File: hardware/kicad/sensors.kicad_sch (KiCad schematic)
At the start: 0 parts

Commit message: kicad: chunk #5a - SEN66 reference footprint + 4 zip-tie NPTH + J3 socket
Adds the SEN66 (Sensirion SEN66-SIN-T, MPN 3.001.030, EAN N/A) connection
to the sensors sub-sheet and lays out the mechanical reference + retention
on the PCB. Resolves 2 of 6 expected ERC pin_not_connected (I2C_SDA, SCL).

Schematic (sensors.kicad_sch):
  J3 = JST GH 6-pin board socket (SM06B-GHS-TB compatible). Wiring per
  SEN6x datasheet Table 16: 1=VDD->+3V3, 2=GND, 3=SDA, 4=SCL,
  5=GND-redundant, 6=VDD-redundant (pins 5/6 internally tied to 1/2 in
  the SEN6x). Local 100 nF decoupling (C10) on the cable side of J3.

Custom PCB footprints:
  oas:SEN66_Mechanical_Reference - 55.2 x 25.6 mm body outline on F.Fab +
    F.SilkS, inlet/outlet markers at exact STEP-derived positions
    (inlet 1 obround at SEN66-local 10.7/7.4, inlet 2 rect at 10.65/18.85,
    outlet circle dia 20.74 at 42.4/12.8), connector marker on +X short
    edge, dashed sealing-divider hint at SEN66-local X=26. Mechanical-
    only, no pads (sensor is held by zip-ties, not soldered).
  oas:ZipTieHole_3mm_NPTH - reusable NPTH hole (3 mm drill, 4 mm silk
    ring, no copper) for ZT1..ZT4 mounting holes.

PCB placement (v0.7 of this chunk after user-iterated refinements):
  - SEN66 anchor at PCB (12, 25), rotation 90 CW. Body X 12..37.6,
    Y -30.2..25 -- clears all cutout zones (lowest cutout Y=27.2 at C2)
    by 2.2 mm. Long axis radial, connector edge at PCB top of body.
    Cross-sector placement (per user OK).
  - Zip-tie holes ZT1..ZT4 at SEN66-local (22, +-3) and (30, +-3).
    Both X positions in safe corridor [19.22, 31.03] so a 2 mm
    zip-tie band centred at each X passes over the SEN66 body
    without covering any inlet or outlet on the air-side face.
    PCB-global: ZT1=(9,3), ZT2=(40.6,3), ZT3=(9,-5), ZT4=(40.6,-5).
    All clear of cable pass-through hole (Phi 12) at origin.
  - J3 at PCB (48, 7), rotation 90 (vertical pin row, plug socket
    opening faces SEN66). 10.4 mm to body right edge for cable be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
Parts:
- added C10: 100nF, symbol Device:C
- added J3: JST SM06B-GHS-TB (SEN66-SIN-T, MPN 3.001.030; TME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, symbol Connector_Generic:Conn_01x06
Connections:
- new net +3V3: C10.1, J3.1 (Pin_1), J3.6 (Pin_6)
- new net GND: C10.2, J3.2 (Pin_2), J3.5 (Pin_5)
- new net I2C_SCL: J3.4 (Pin_4)
- new net I2C_SDA: J3.3 (Pin_3)

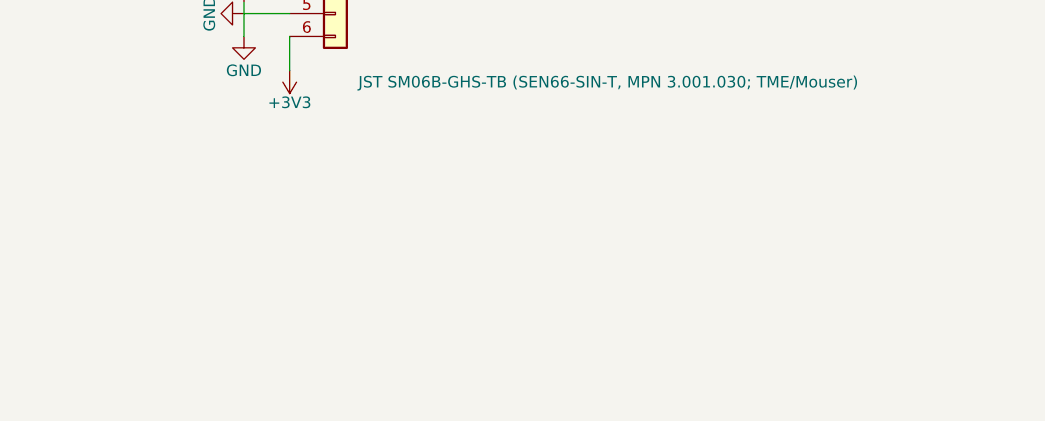
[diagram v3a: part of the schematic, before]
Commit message: kicad: chunk #5b - LD2410 mmWave radar (J4 + C11) in sensors.kicad_sch
Adds the HLK-LD2410B presence radar connection to the sensors sub-sheet.
Resolves 4 of the 5 ERC issues that remained after chunk #5a:
- 3 sensors-side hier labels (LD2410_OUT, UART_TX, UART_RX) now exist
  and are wired through to the MCU side
- 3 root-sheet inter-sheet wires bind the matching sensors/mcu sheet
  pins so KiCad ERC sees the cross-sheet nets as electrically continuous

Schematic content (sensors.kicad_sch):
  J4 — JST SM05B-GHS-TB 5-pin board socket, mates with HLK-LD2410B
       stock cable. Pinout (per HiLink LD2410B datasheet):
         Pin 1: VCC (+5V from U1)
         Pin 2: GND
         Pin 3: TX  -> UART_RX (LD2410 output drives MCU GPIO 17)
         Pin 4: RX  <- UART_TX (MCU GPIO 16 drives LD2410 input)
         Pin 5: OUT -> LD2410_OUT (presence interrupt to MCU GPIO 2)
       Logic levels are 3.3 V TTL on TX/RX/OUT despite the 5 V supply,
       so the ESP32-C6 sees compatible levels without a level shifter.
  C11 — 100 nF 0402 X7R, local decoupling between +5V and GND at the
       J4 plug. Damps cable transient ringing on the +5V rail.

New schematic library symbols loaded verbatim from KiCad 10 stock libs
via the new `_read_kicad_lib_symbol()` helper (which prefixes the
symbol name with its library nickname and re-indents to fit our
embedded lib_symbols block):
  Connector_Generic:Conn_01x05
  power:+5V

New schematic helper:
  `_sch_conn_01x05()` — emits a 5-pin Conn_01x05 instance. Mirrors
  `_sch_conn_01x06` with one fewer pin and the Value property anchored
  at Y+10.16 (vs Y+12.7 for the 6-pin variant) to track the bottom
  pin's new Y position.

Root sheet (oas.kicad_sch) gains 3 new inter-sheet wire groups:
  - LD2410_OUT : sensors (88.9, 95.25) -> MCU left (101.6, 57.15) via
                 a vertical leg at X=100.33.
  - UART_TX    : sensors (88.9, 97.79) -> MCU right (139.7, 52.07) via
                 a vertical leg at X=143.51 (past the io block's east
 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
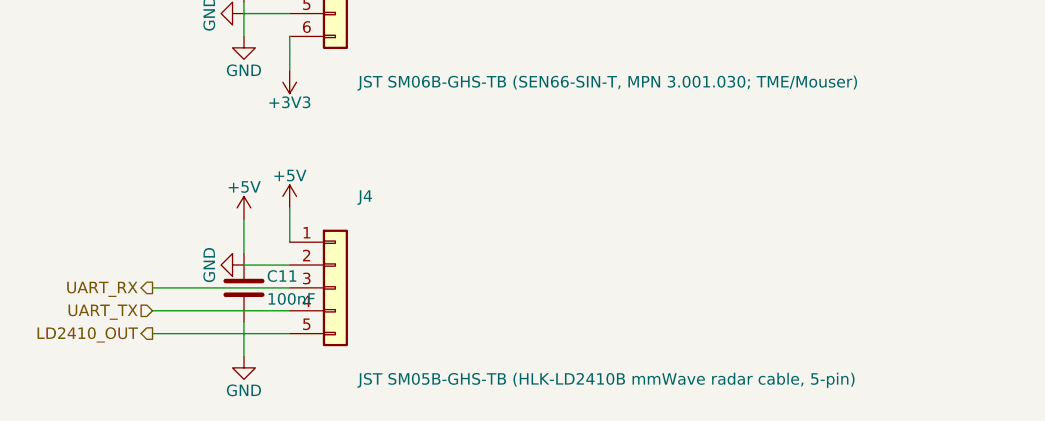
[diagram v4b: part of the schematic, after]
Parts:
- added C11: 100nF, symbol Device:C
- added J4: JST SM05B-GHS-TB (HLK-LD2410B mmWave radar cable,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, symbol Connector_Generic:Conn_01x05
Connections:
- net GND: now also C11.2, J4.2 (Pin_2)
- new net +5V: C11.1, J4.1 (Pin_1)
- new net LD2410_OUT: J4.5 (Pin_5)
- new net UART_RX: J4.3 (Pin_3)
- new net UART_TX: J4.4 (Pin_4)

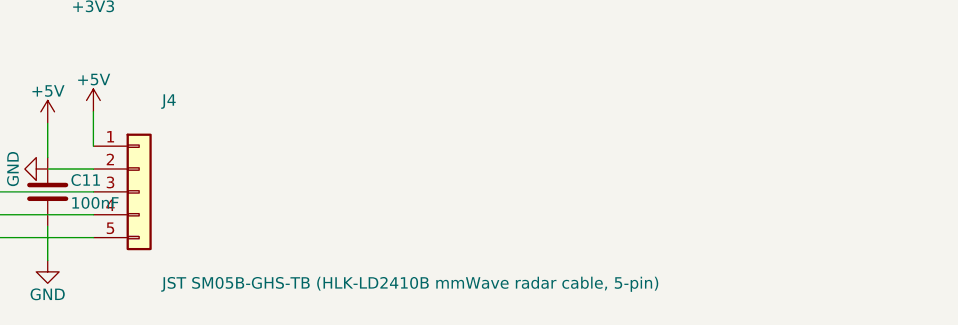
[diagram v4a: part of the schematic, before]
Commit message: kicad: chunk #5b refinement - LD2410 mounts as soldered daughterboard
User-driven decision after researching how community / commercial
products physically mount the HLK-LD2410:

  Apollo MSR-2  - LD2410B integrated on/with main PCB, antenna toward
                  perforated cover
  jonnybergdahl Sensor_LD2410B - 3D-printed slot, antenna toward front
  p2baron Thingiverse 5782554  - same pattern
  HiLink datasheet §5.5         - "antenna facing the area to be
                                  detected, surrounding area open and
                                  unobstructed"; "cannot contain metal
                                  materials" (FR4 copper pour counts)

Universal pattern: antenna face oriented TOWARD the user (through the
cover material). Zero documented projects mount the LD2410 with the
host PCB *between* the antenna and the user.

Concrete mounting change for OAS:
- LD2410 is now a soldered daughterboard. The HLK-LD2410B's onboard
  1.27 mm pin row passes through J4's through-hole pads on the OAS
  PCB; the pins are soldered from the OAS PCB bottom side. The solder
  joints provide BOTH electrical and mechanical retention -- no JST
  cable, no zip-tie, no bracket. Antenna face points UP (away from the
  OAS PCB, toward the AK-N-94 perforated cover) so the radar beam
  radiates through the cover into the room.

Schematic-side changes (sensors.kicad_sch):
- J4 Value field changed from "JST SM05B-GHS-TB ..." (SMD socket) to
  "1x5 P1.27mm through-hole header (HLK-LD2410B daughterboard,
  soldered)". The Conn_01x05 symbol is unchanged -- the difference
  vs the JST-GH variant is purely the PCB footprint association,
  which lands in chunk #7 (PCB placement).
- Chunk #5b docstring rewritten to reflect the mounting strategy +
  cite the HiLink datasheet rationale and the community/commercial
  precedents.

No KiCad output changes besides J4's Value text + docstring/comment
text inside the generator. DRC: 0 violations. ERC: 3 unchanged (1
expected error 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
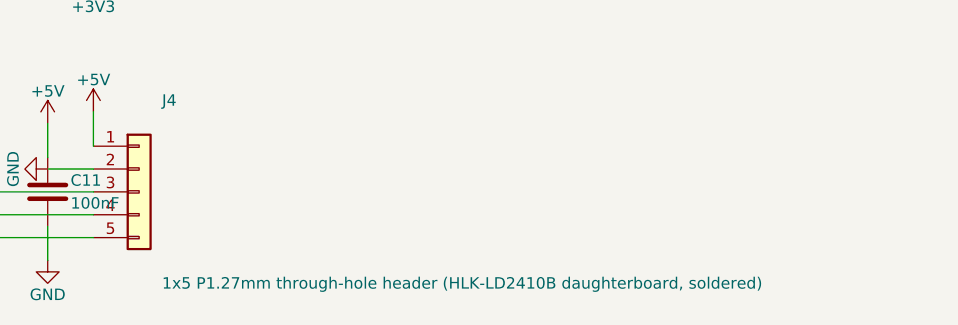
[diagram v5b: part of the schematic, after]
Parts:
- J4: value JST SM05B-GHS-TB (HLK-LD2410B mmWave radar cable, 5-pin) -> 1x5 P1.27mm through-hole header (HLK-LD2410B daughterboard, soldered)
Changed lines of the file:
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@@
         			)
         		)
-        		(property "Value" "JST SM05B-GHS-TB (HLK-LD2410B mmWave radar cable, 5-pin)"
+        		(property "Value" "1x5 P1.27mm through-hole header (HLK-LD2410B daughterboard, soldered)"
         			(at 182.88 156.21 0)
         			(effects

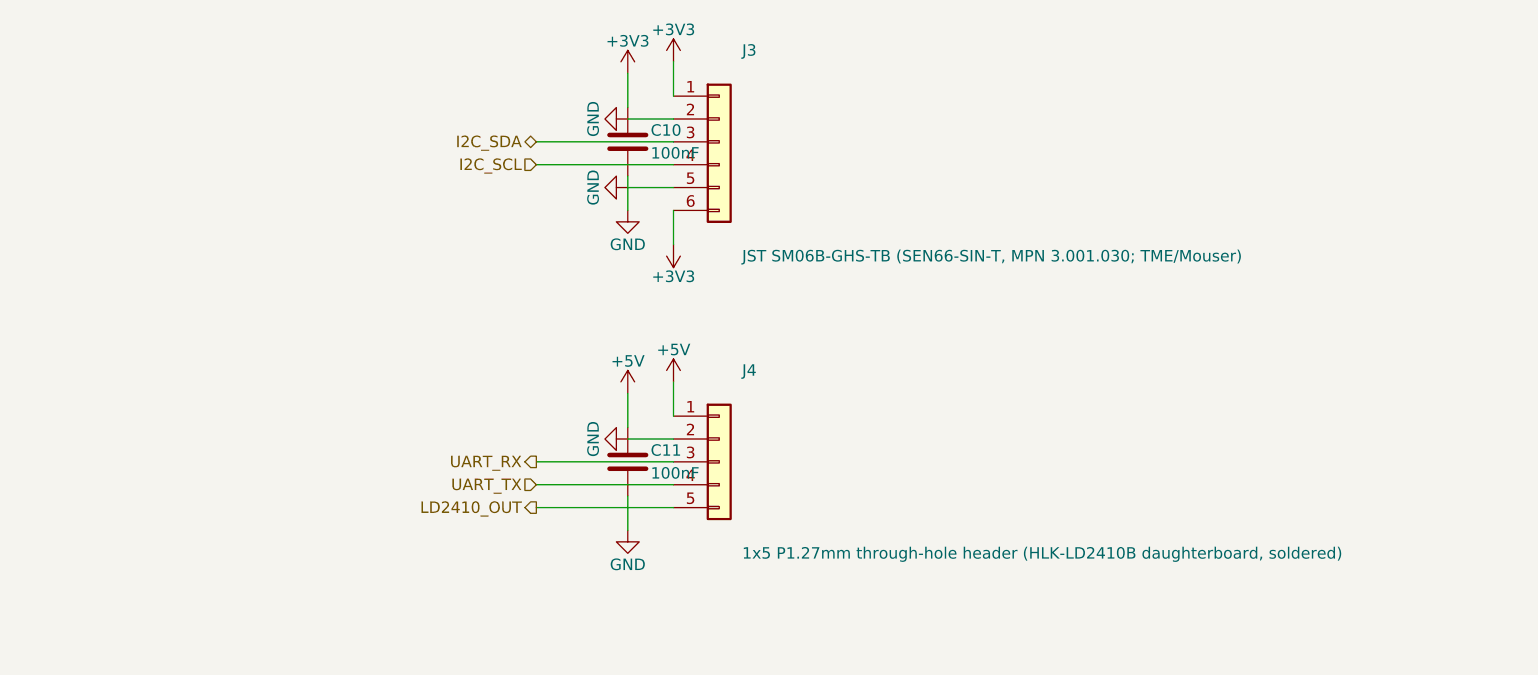
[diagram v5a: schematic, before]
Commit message: kicad: chunk #5c - MIKROE-2462 NFC Tag 2 Click (U4 + C12)
Final sensors-sub-sheet chunk: the NFC tag connection. Closes the
last expected ERC hier-label warning (NFC_FD).

Architecture change vs the v0.6 plan (a discrete NXP NT3H2x11 SMD +
custom PCB-trace NFC antenna): we instead host the NFC tag on a
MikroElektronika "NFC Tag 2 Click" (MIKROE-2462) -- NT3H2111 NTAG
I2C plus + onboard pre-tuned PCB antenna + mikroBUS 2x8 male header.
The Click board plugs into a 2x8 female pin socket on the OAS PCB
(P2.54 mm). Pre-tuned antenna eliminates the NXP AN11203 antenna-
design sub-project entirely; mikroBUS form factor is easy to source
(TME / Distrelec / Farnell / RS in the EU) and easy to swap or
remove for service via the pin-only mating.

Research summary (May 2026) drove the choice:
- MIKROE-2462 (NT3H2111 + antenna, mikroBUS, ~12-15 USD): selected.
- MIKROE-3659 (ST25DV16K, mikroBUS): strong runner-up; better EU
  stock but less DIY/ESPHome precedent.
- M5Stack U216, DFRobot DFR0231: rejected -- both are NFC readers
  (ST25R3916, PN532), not writeable tags.
- Adafruit NTAG I2C breakout: confirmed non-existent in catalog.
- Generic AliExpress NT3H2x11 breakouts: no citable listing meeting
  the Module Identification rule.

Schematic content (sensors.kicad_sch):
  U4 = Connector_Generic:Conn_02x08_Top_Bottom (placeholder for the
       mikroBUS socket; PCB footprint = 2x8 female pin socket P2.54
       mm, lands in chunk #7). The Top_Bottom variant of Conn_02x08
       has pins 1-8 down the LEFT column and 9-16 down the RIGHT
       column, exactly matching the mikroBUS pin-numbering convention.
       Only 6 pins are connected (the other 10 get no_connect markers):
         mikroBUS  7 (+3.3V) -> +3V3 power flag
         mikroBUS  8 (GND)   -> GND power flag
         mikroBUS 10 (INT)   -> NFC_FD hier label (output direction)
                                going to MCU GPIO 3
         mikroBUS 13 (SCL)   -> I2C_SCL hier label
         mikroBUS 14 (SDA)   -> I2C_SDA 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
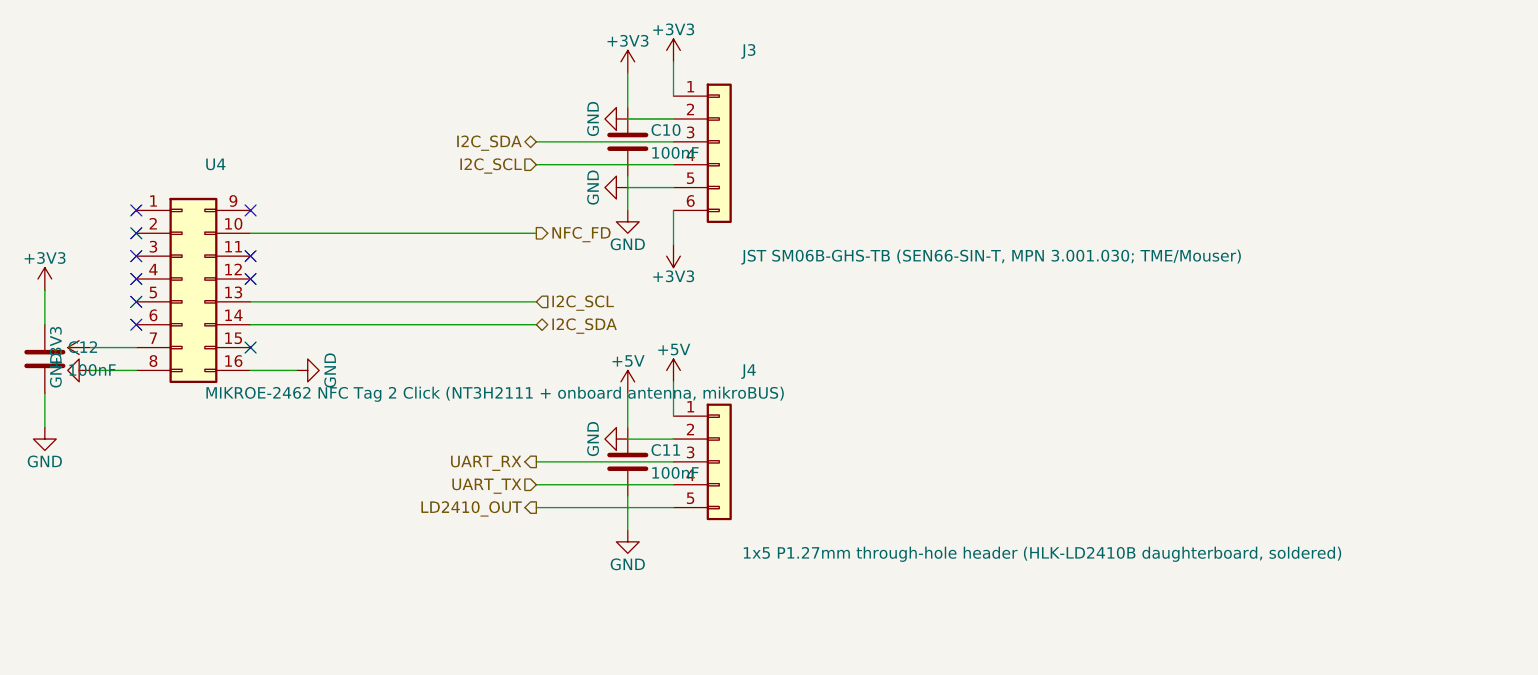
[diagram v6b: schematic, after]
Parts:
- added C12: 100nF, symbol Device:C
- added U4: MIKROE-2462 NFC Tag 2 Click (NT3H2111 + onboard a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, symbol Connector_Generic:Conn_02x08_Top_Bottom
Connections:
- net +3V3: now also C12.1, U4.7 (Pin_7)
- net GND: now also C12.2, U4.16 (Pin_16), U4.8 (Pin_8)
- net I2C_SCL: now also U4.13 (Pin_13)
- net I2C_SDA: now also U4.14 (Pin_14)
- new net NFC_FD: U4.10 (Pin_10)
- no-connect marks 0 -> 10

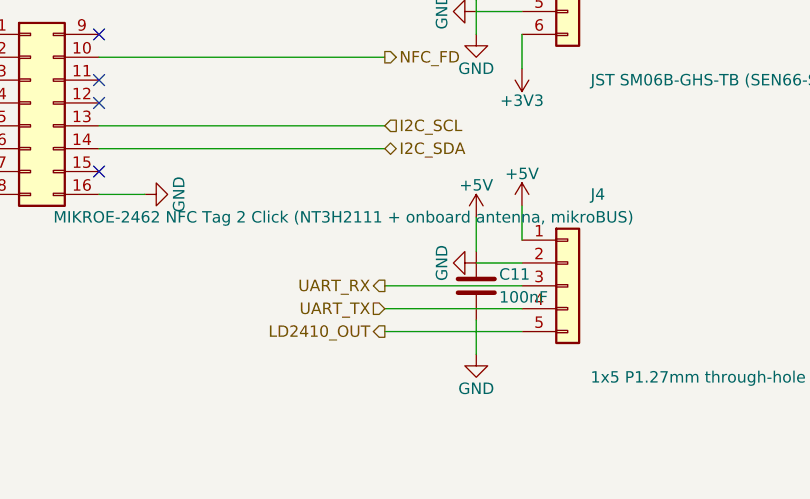
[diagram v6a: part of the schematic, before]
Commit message: kicad: CRITICAL fix J4 pin order to match HLK-LD2410B datasheet
Per HiLink HLK-LD2410B datasheet V1.04 (FCC-filed), Table 1 page 7:
  Pin 1 = OUT, Pin 2 = UART_Tx, Pin 3 = UART_Rx, Pin 4 = GND, Pin 5 = VCC

Previous J4 mapping was reversed end-for-end (pin 1 = VCC, pin 5 = OUT).
Power/GND coincidentally worked by symmetry, but UART direction was
swapped (both sides driving inputs / both sides driving outputs - bus
contention) and OUT signal landed at the wrong physical pin.

If the previous (incorrect) footprint were built and a real LD2410B
soldered in, the radar would have been powered correctly by accident
but the UART would not function and the OUT presence interrupt would
land on the +5V pad. UART_RX/TX were wired symmetrically against the
LD2410's own pin 2 (Tx output) and pin 3 (Rx input), driving them in
the opposite of the intended direction.

C11 (100 nF VCC decoupling) repositioned below the new pin 5 (VCC,
bottom of pin row) so its top pin shares J4 pin 5's +5V flag and its
bottom pin terminates at a local GND flag.

Schematic-only change. PCB pads physical positions are unchanged
(J4 footprint stays where it is); only the net assigned to each pad
moves. DRC=0, ERC=0.

Discovered in independent code review (hardware/components/hlk-ld2410b.md
Discrepancy #1, _overall-review-v0.15.7.md).

Co-Authored-By: Claude Opus 4.7 (1M context) <noreply@anthropic.com>
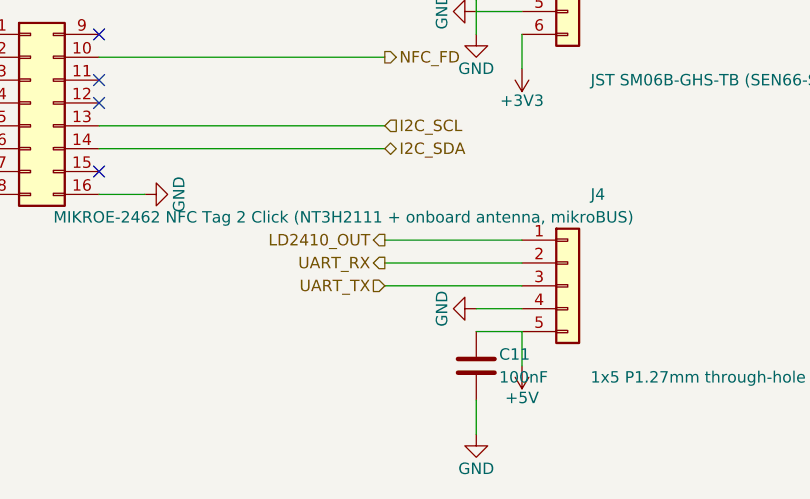
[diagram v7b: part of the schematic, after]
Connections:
- net +5V: now also J4.5 (Pin_5); no longer J4.1 (Pin_1)
- net GND: now also J4.4 (Pin_4); no longer J4.2 (Pin_2)
- net LD2410_OUT: now also J4.1 (Pin_1); no longer J4.5 (Pin_5)
- net UART_RX: now also J4.2 (Pin_2); no longer J4.3 (Pin_3)
- net UART_TX: now also J4.3 (Pin_3); no longer J4.4 (Pin_4)
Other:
- moved on the sheet: C11
